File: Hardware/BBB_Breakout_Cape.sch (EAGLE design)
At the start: 1 part

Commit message: board ready for review
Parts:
- added C1: (no value), SparkFun-Capacitors:0.1UF-25V(+80/-20%)(0603)
- added FRAME1: FRAME-LETTER, SparkFun-Aesthetics:FRAME-LETTER
- added JP1, JP2: (no value), SparkFun-Passives:JUMPER-2SMD-NO
- added LOGO2: OSHW-LOGOS, SparkFun-Aesthetics:OSHW-LOGOS
- added LOGO3: SFE_LOGO_NAME_FLAME.1_INCH, SparkFun-Aesthetics:SFE_LOGO_NAME_FLAME.1_INCH
- added R1, R2, R3, R4, R5: (no value), SparkFun-Resistors:4.7KOHM1/10W1%(0603)
- added R6: (no value), SparkFun-Resistors:10KOHM1/10W1%(0603)0603
- added SJ1: (no value), SparkFun-Passives:SOLDERJUMPER_2WAYPASTE1&2&3
- added SJ2: (no value), SparkFun-Passives:SOLDERJUMPER_2WAYPASTE2&3
- added U$2, U$3, U$4, U$5: M23, SparkFun-Connectors:M23
- added U1: EEPROM-I2CSMD, SparkFun-DigitalIC:EEPROM-I2CSMD
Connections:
- new net 3.3V: C1.1, R1.2, R2.2, R3.2, SJ1.2, SJ2.1, U1.VCC
- new net A0: JP1.1, R3.1, U1.A0
- new net A1: JP2.1, R2.1, U1.A1
- new net GND: C1.2, JP1.2, JP2.2, SJ2.3, U$1P8.DGND@1, U$1P8.DGND@2, U$1P9.DGND@1, U$1P9.DGND@2, U$1P9.DGND@3, U$1P9.DGND@4, U$1P9.DGND@5, U$1P9.DGND@6, U$2.24, U$3.24, U$4.2, U$4.24, U$4.3, U$5.2, U$5.24, U$5.3, U1.VSS
- new net N$1: R6.1, U1.WP
- new net N$10: R4.2, SJ1.3
- new net N$11: R5.2, SJ1.1
- new net N$12: U$1P8.GPIO_78, U$2.6
- new net N$13: U$1P8.GPIO_8, U$2.7
- new net N$14: U$1P8.GPIO_9, U$2.8
- new net N$15: U$1P8.GPIO_10, U$2.9
- new net N$16: U$1P8.GPIO_87, U$2.10
- new net N$17: U$1P8.GPIO_86, U$2.11
- new net N$18: U$1P8.GPIO_32, U$2.12
- new net N$19: U$1P8.GPIO_36, U$2.13
- new net N$2: U$1P8.GPIO_70, U$2.2
- new net N$20: U$1P8.GPIO_62, U$2.14
- new net N$21: U$1P8.GPIO_22, U$2.15
- new net N$22: U$1P8.GPIO_27, U$2.16
- new net N$23: U$1P8.GPIO_47, U$2.17
- new net N$24: U$1P8.GPIO_23, U$2.18
- new net N$25: U$1P8.GPIO_45, U$2.19
- new net N$26: U$1P8.GPIO_69, U$2.20
- new net N$27: U$1P8.GPIO_66, U$2.21
- new net N$28: U$1P8.GPIO_34, U$2.22
- new net N$29: U$1P8.GPIO_38, U$2.23
- new net N$3: R6.2, SJ2.2
- new net N$31: U$1P8.GPIO_71, U$3.2
- new net N$32: U$1P8.GPIO_73, U$3.3
- new net N$33: U$1P8.GPIO_75, U$3.4
- new net N$34: U$1P8.GPIO_77, U$3.5
- new net N$35: U$1P8.GPIO_79, U$3.6
- new net N$36: U$1P8.GPIO_80, U$3.7
- new net N$37: U$1P8.GPIO_81, U$3.8
- new net N$38: U$1P8.GPIO_11, U$3.9
- new net N$39: U$1P8.GPIO_89, U$3.10
- new net N$4: U$1P8.GPIO_72, U$2.3
- new net N$40: U$1P8.GPIO_88, U$3.11
- new net N$41: U$1P8.GPIO_61, U$3.12
- new net N$42: U$1P8.GPIO_33, U$3.13
- new net N$43: U$1P8.GPIO_37, U$3.14
- new net N$44: U$1P8.GPIO_63, U$3.15
- new net N$45: U$1P8.GPIO_65, U$3.16
- new net N$46: U$1P8.GPIO_46, U$3.17
- new net N$47: U$1P8.GPIO_26, U$3.18
- new net N$48: U$1P8.GPIO_44, U$3.19
- new net N$49: U$1P8.GPIO_68, U$3.20
- new net N$5: U$1P8.GPIO_74, U$2.4
- new net N$50: U$1P8.GPIO_67, U$3.21
- new net N$51: U$1P8.GPIO_35, U$3.22
- new net N$52: U$1P8.GPIO_39, U$3.23
- new net N$56: U$1P9.GPIO_7, U$5.4
- new net N$57: U$1P9.AIN1, U$5.5
- new net N$58: U$1P9.AIN3, U$5.6
- new net N$59: U$1P9.AIN5, U$5.7
- new net N$6: R1.1, U1.A2
- new net N$60: U$1P9.GNDA_ADC, U$5.8
- new net N$61: U$1P9.VDD_ADC, U$5.9
- new net N$62: U$1P9.GPIO_122, U$5.10
- new net N$63: U$1P9.GPIO_123, U$5.11
- new net N$64: U$1P9.GPIO_14, U$5.12
- new net N$65: U$1P9.GPIO_15, U$5.13
- new net N$66: U$1P9.GPIO_2, U$5.14
- new net N$68: U$1P9.GPIO_5, U$5.16
- new net N$69: U$1P9.GPIO_51, U$5.17
- new net N$70: U$1P9.GPIO_40, U$5.18
- new net N$71: U$1P9.GPIO_60, U$5.19
- new net N$72: U$1P9.SYS_RESET!N, U$5.20
- new net N$73: U$1P9.SYS_5V@2, U$5.21
- new net N$74: U$1P9.VDD_5V@2, U$5.22
- new net N$75: U$1P9.VDD_3V3@2, U$5.23
- new net N$79: U$1P9.GPIO_20, U$4.4
- new net N$80: U$1P9.AIN0, U$4.5
- new net N$81: U$1P9.AIN2, U$4.6
- new net N$82: U$1P9.AIN6, U$4.7
- new net N$83: U$1P9.AIN4, U$4.8
- new net N$84: U$1P9.GPIO_120, U$4.9
- new net N$85: U$1P9.GPIO_121, U$4.10
- new net N$86: U$1P9.GPIO_125, U$4.11
- new net N$87: U$1P9.GPIO_117, U$4.12
- new net N$88: U$1P9.GPIO_49, U$4.13
- new net N$89: U$1P9.GPIO_3, U$4.14
- new net N$9: U$1P8.GPIO_76, U$2.5
- new net N$91: U$1P9.GPIO_4, U$4.16
- new net N$92: U$1P9.GPIO_48, U$4.17
- new net N$93: U$1P9.GPIO_31, U$4.18
- new net N$94: U$1P9.GPIO_30, U$4.19
- new net N$95: U$1P9.PWR_BUT, U$4.20
- new net N$96: U$1P9.SYS_5V@1, U$4.21
- new net N$97: U$1P9.VDD_5V@1, U$4.22
- new net N$98: U$1P9.VDD_3V3@1, U$4.23
- new net SCL: R5.1, U$1P9.I2C2_SCL, U$4.15, U1.SCL
- new net SDA: R4.1, U$1P9.I2C2_SDA, U$5.15, U1.SDA

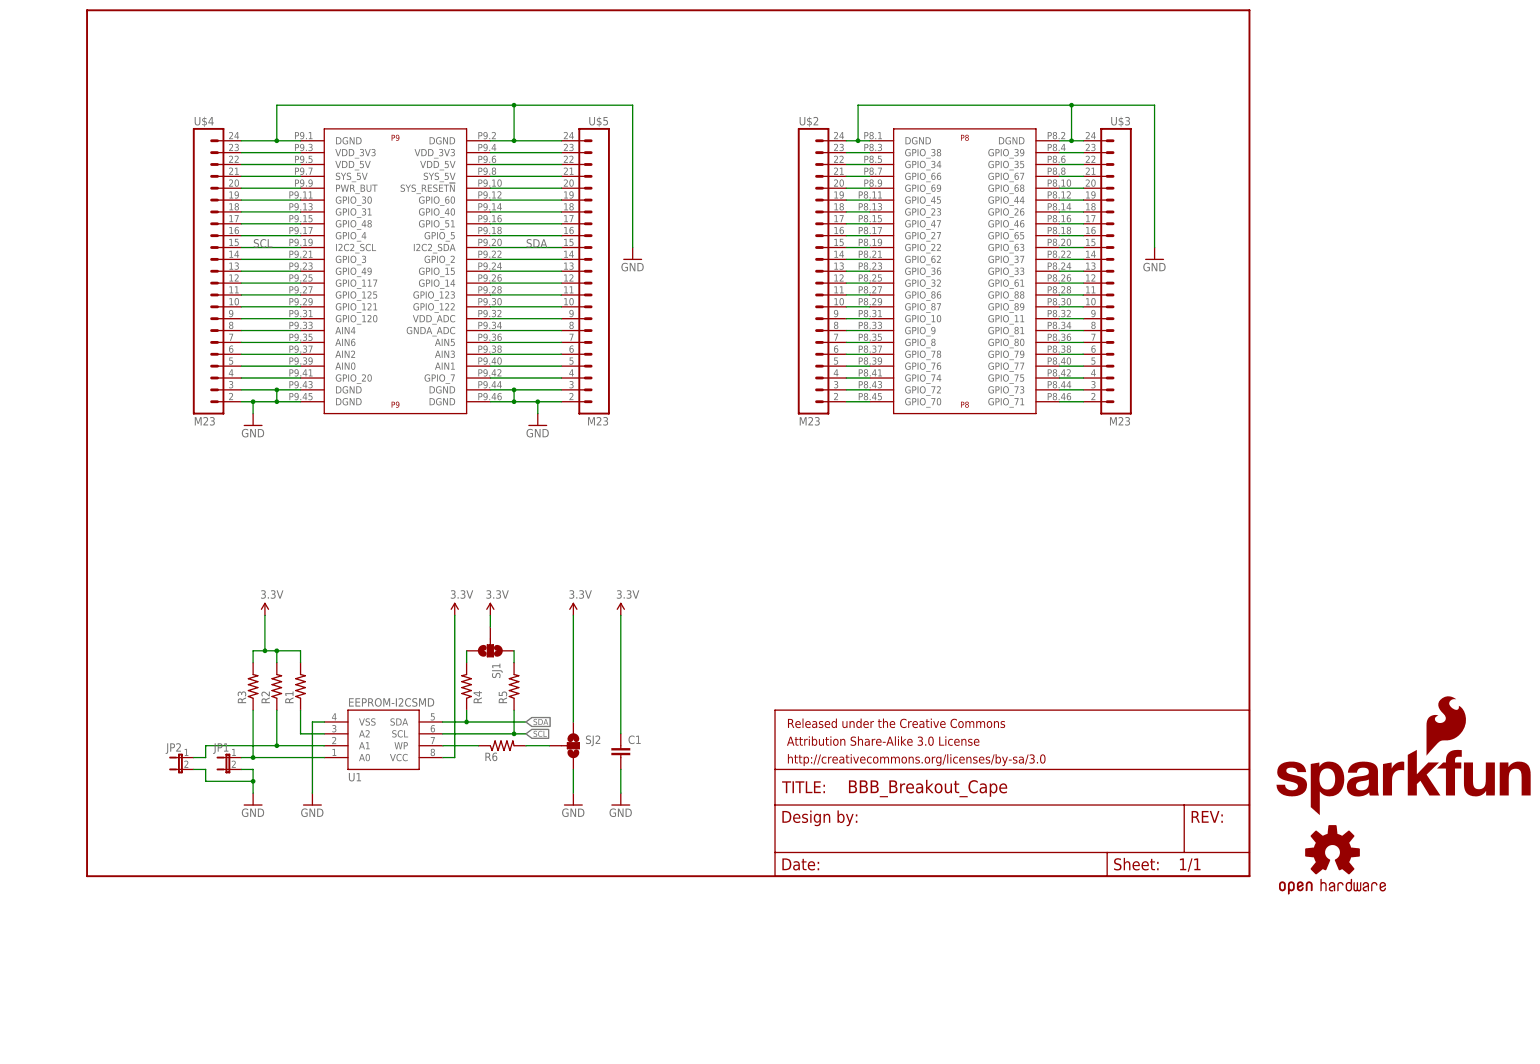
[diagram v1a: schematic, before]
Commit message: Updated labels and corrected silk on bottom layer
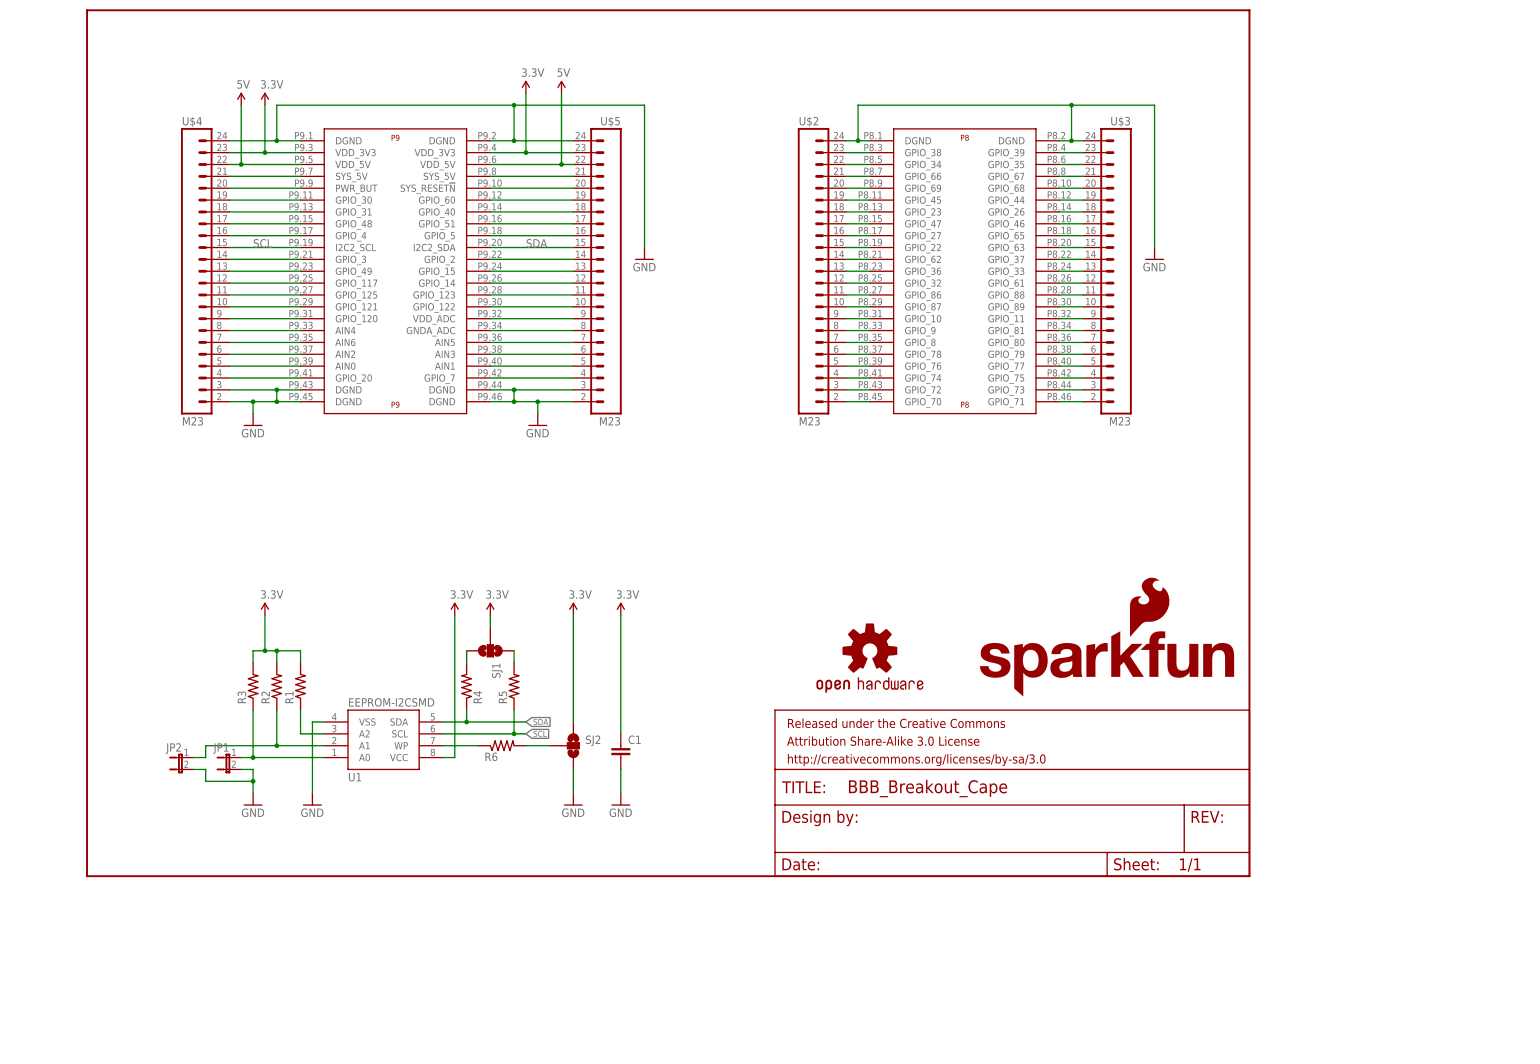
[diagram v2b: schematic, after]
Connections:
- removed net N$74: U$1P9.VDD_5V@2, U$5.22
- removed net N$75: U$1P9.VDD_3V3@2, U$5.23
- removed net N$97: U$1P9.VDD_5V@1, U$4.22
- removed net N$98: U$1P9.VDD_3V3@1, U$4.23
- new net 5V: U$1P9.VDD_5V@1, U$1P9.VDD_5V@2, U$4.22, U$5.22
- net 3.3V: now also U$1P9.VDD_3V3@1, U$1P9.VDD_3V3@2, U$4.23, U$5.23
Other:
- moved on the sheet: U$4, U$5

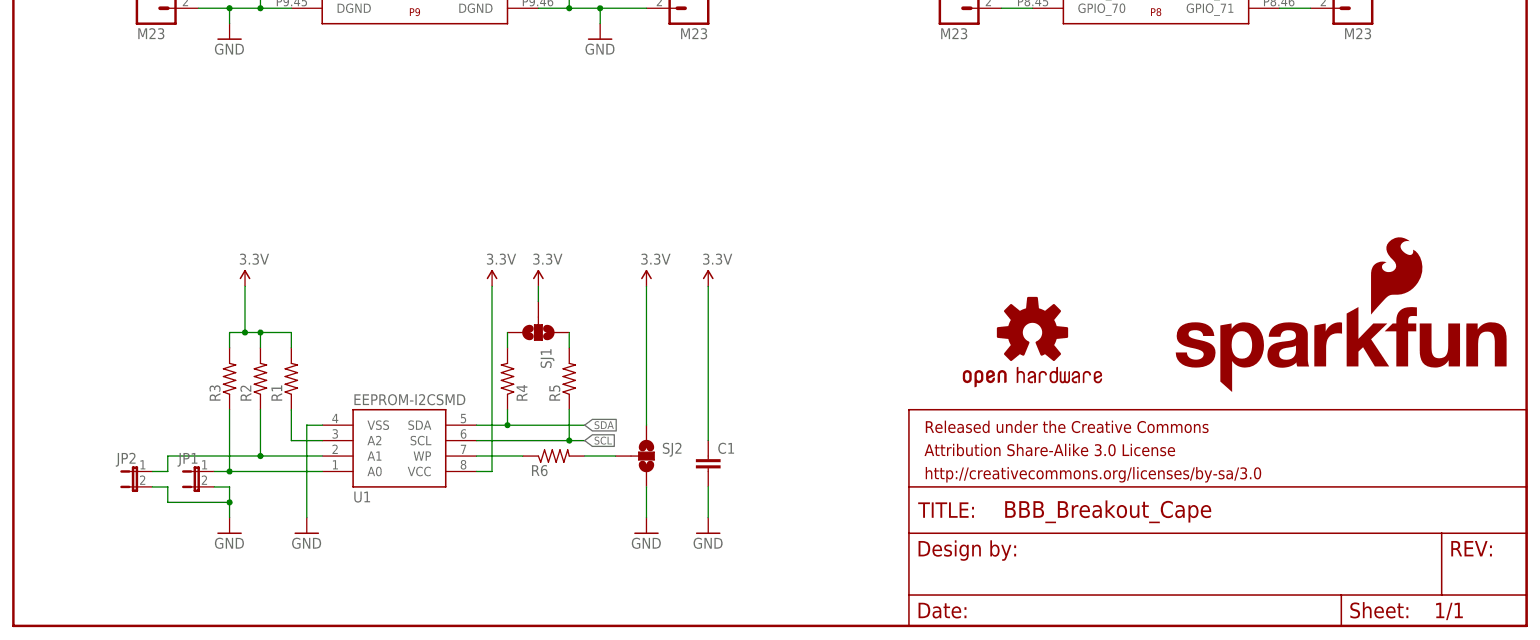
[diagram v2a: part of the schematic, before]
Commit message: added labels and corrected WP jumper to eliminate possible short.
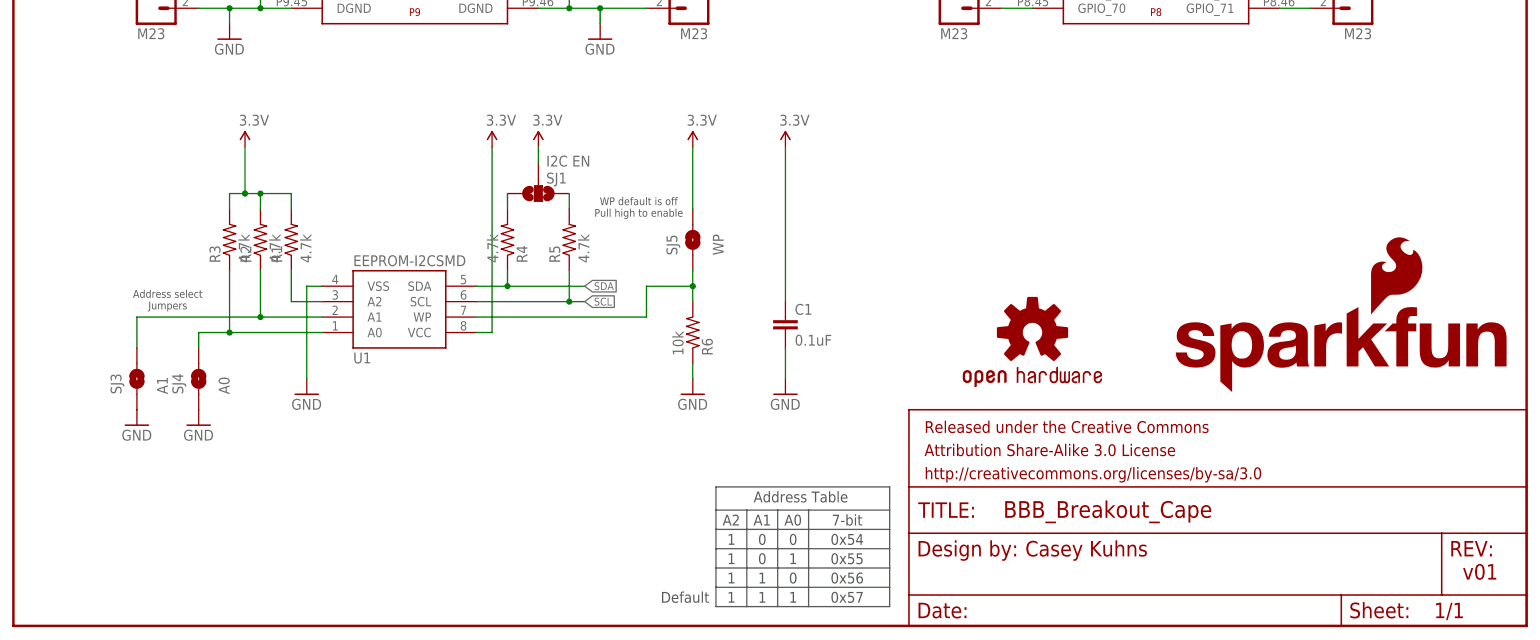
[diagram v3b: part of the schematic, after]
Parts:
- removed JP1, JP2: (no value), SparkFun-Passives:JUMPER-2SMD-NO
- removed SJ2: (no value), SparkFun-Passives:SOLDERJUMPER_2WAYPASTE2&3
- added SJ3: A1, SparkFun-Passives:SOLDERJUMPERNO
- added SJ4: A0, SparkFun-Passives:SOLDERJUMPERNO
- added SJ5: WP, SparkFun-Passives:SOLDERJUMPERNO
- C1: value (none) -> 0.1uF
- R1, R2, R3, R4, R5: value (none) -> 4.7k
- R6: value (none) -> 10k
- SJ1: value (none) -> I2C EN
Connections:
- removed net N$3: R6.2, SJ2.2
- net 3.3V: now also SJ5.2; no longer SJ2.1
- net A0: now also SJ4.2; no longer JP1.1
- net A1: now also SJ3.2; no longer JP2.1
- net GND: now also R6.1, SJ3.1, SJ4.1; no longer JP1.2, JP2.2, SJ2.3
- net N$1: now also R6.2, SJ5.1; no longer R6.1
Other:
- note added: "0"
- note added: "0x54"
- note added: "0x55"
- note added: "0x56"
- note added: "0x57"
- note added: "1"
- note added: "7-bit"
- note added: "A0"
- note added: "A1"
- note added: "A2"
- note added: "Address Table"
- note added: "Address select Jumpers"
- note added: "Casey Kuhns"
- note added: "Default"
- note added: "WP default is off Pull high to enable"
- note added: "v01"
- moved on the sheet: C1, R1, R2, R3, R4, R5, R6, SJ1, U1

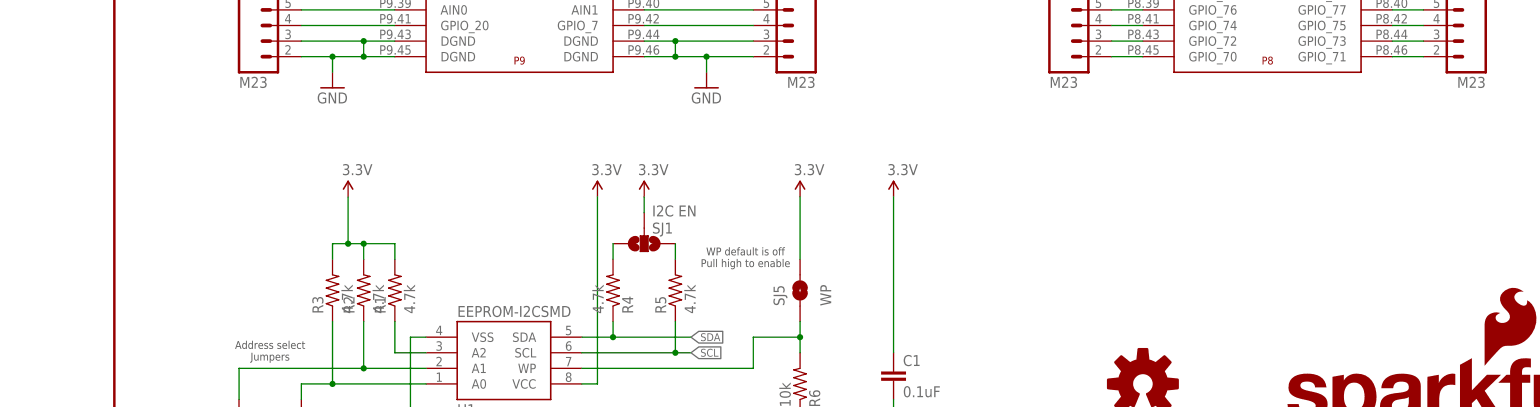
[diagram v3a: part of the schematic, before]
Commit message: added LEDS
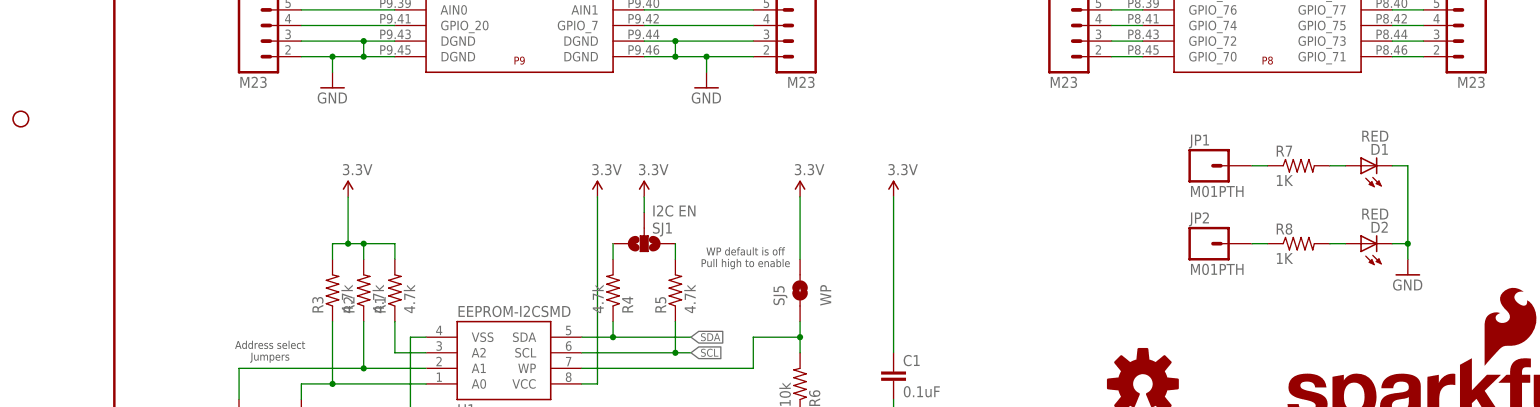
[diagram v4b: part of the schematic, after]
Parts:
- added D1, D2: RED, SparkFun-LED:LED-RED0603
- added JP1, JP2: M01PTH, SparkFun-Connectors:M01PTH
- added R7, R8: 1K, SparkFun-Resistors:1KOHM1/10W1%(0603)
- added STANDOFF1: STAND-OFF, SparkFun-Electromechanical:STAND-OFF
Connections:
- new net N$3: D1.A, R7.2
- new net N$30: JP2.1, R8.1
- new net N$7: D2.A, R8.2
- new net N$8: JP1.1, R7.1
- net GND: now also D1.C, D2.C
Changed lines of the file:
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@@
 <part name="GND9" library="SparkFun-Aesthetics" deviceset="GND" device=""/>
 <part name="SJ5" library="SparkFun-Passives" deviceset="SOLDERJUMPER" device="NO" value="WP"/>
+<part name="D1" library="SparkFun-LED" deviceset="LED-RED" device="0603" value="RED"/>
+<part name="D2" library="SparkFun-LED" deviceset="LED-RED" device="0603" value="RED"/>
+<part name="R7" library="SparkFun-Resistors" deviceset="1KOHM1/10W1%(0603)" device="" value="1K"/>
+<part name="R8" library="SparkFun-Resistors" deviceset="1KOHM1/10W1%(0603)" device="" value="1K"/>
+<part name="GND10" library="SparkFun-Aesthetics" deviceset="GND" device=""/>
+<part name="JP1" library="SparkFun-Connectors" deviceset="M01" device="PTH"/>
+<part name="JP2" library="SparkFun-Connectors" deviceset="M01" device="PTH"/>
+<part name="STANDOFF1" library="SparkFun-Electromechanical" deviceset="STAND-OFF" device=""/>
 </parts>
 <sheets>
@@
 <instance part="GND9" gate="1" x="20.32" y="33.02"/>
 <instance part="SJ5" gate="1" x="111.76" y="63.5" rot="R90"/>
+<instance part="D1" gate="G$1" x="203.2" y="83.82" rot="R90"/>
+<instance part="D2" gate="G$1" x="203.2" y="71.12" rot="R90"/>
+<instance part="R7" gate="G$1" x="193.04" y="83.82"/>
+<instance part="R8" gate="G$1" x="193.04" y="71.12"/>
+<instance part="GND10" gate="1" x="210.82" y="66.04"/>
+<instance part="JP1" gate="G$1" x="177.8" y="83.82"/>
+<instance part="JP2" gate="G$1" x="177.8" y="71.12"/>
+<instance part="STANDOFF1" gate="G$1" x="-15.24" y="91.44"/>
 </instances>
 <busses>
@@
 <pinref part="GND9" gate="1" pin="GND"/>
 </segment>
+<segment>
+<pinref part="D1" gate="G$1" pin="C"/>
+<pinref part="GND10" gate="1" pin="GND"/>
+<wire x1="208.28" y1="83.82" x2="210.82" y2="83.82" width="0.1524" layer="91"/>
+<wire x1="210.82" y1="83.82" x2="210.82" y2="71.12" width="0.1524" layer="91"/>
+<pinref part="D2" gate="G$1" pin="C"/>
+<wire x1="210.82" y1="71.12" x2="210.82" y2="68.58" width="0.1524" layer="91"/>
+<wire x1="210.82" y1="71.12" x2="208.28" y2="71.12" width="0.1524" layer="91"/>
+<junction x="210.82" y="71.12"/>
+</segment>
 </net>
 <net name="N$6" class="0">
@@
 </segment>
 </net>
+<net name="N$3" class="0">
+<segment>
+<pinref part="D1" gate="G$1" pin="A"/>
+<pinref part="R7" gate="G$1" pin="2"/>
+<wire x1="198.12" y1="83.82" x2="200.66" y2="83.82" width="0.1524" layer="91"/>
+</segment>
+</net>
+<net name="N$7" class="0">
+<segment>
+<pinref part="D2" gate="G$1" pin="A"/>
+<pinref part="R8" gate="G$1" pin="2"/>
+<wire x1="198.12" y1="71.12" x2="200.66" y2="71.12" width="0.1524" layer="91"/>
+</segment>
+</net>
+<net name="N$8" class="0">
+<segment>
+<pinref part="R7" gate="G$1" pin="1"/>
+<pinref part="JP1" gate="G$1" pin="1"/>
+<wire x1="185.42" y1="83.82" x2="187.96" y2="83.82" width="0.1524" layer="91"/>
+</segment>
+</net>
+<net name="N$30" class="0">
+<segment>
+<pinref part="R8" gate="G$1" pin="1"/>
+<pinref part="JP2" gate="G$1" pin="1"/>
+<wire x1="185.42" y1="71.12" x2="187.96" y2="71.12" width="0.1524" layer="91"/>
+</segment>
+</net>
